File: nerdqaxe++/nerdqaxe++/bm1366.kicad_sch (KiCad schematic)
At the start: 78 parts, among them J2 Conn_01x06, U19 BM1370_mode1, U20 BM1370_mode1, U25 BM1370_mode1, U26 BM1370_mode1, U35 TXU0304PW, U8 25MHz

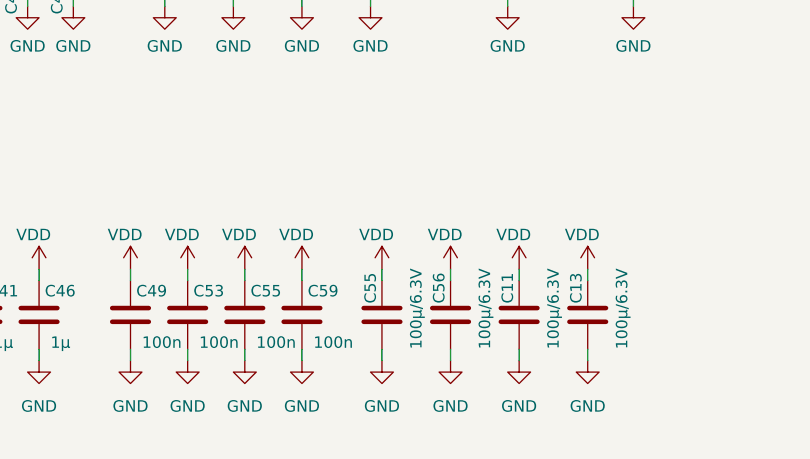
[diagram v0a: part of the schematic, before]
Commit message: removed solderjumpers on ++
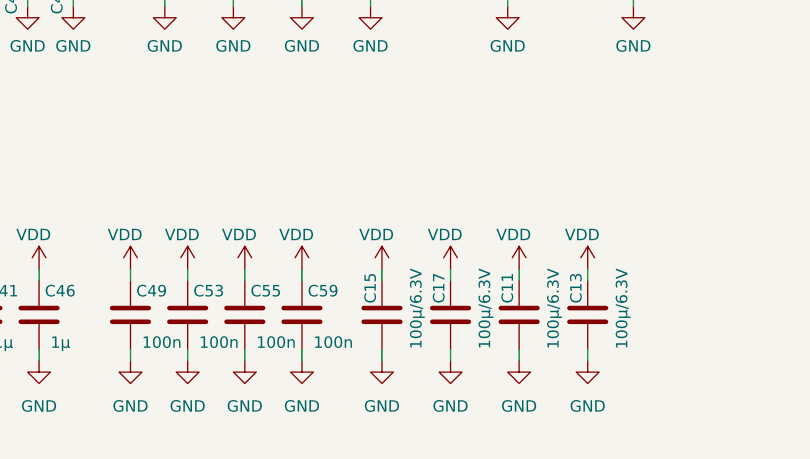
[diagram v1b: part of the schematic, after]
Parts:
- U35: footprint Package_SO:TSSOP-14_4.4x5mm_P0.65mm -> Package_SO:TSSOP-14_4.4x5mm_P0.65mm
- renumbered C55 to C15, C56 to C17
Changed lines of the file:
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@@
 (kicad_sch
-	(version 20231120)
+	(version 20250114)
 	(generator "eeschema")
-	(generator_version "8.0")
+	(generator_version "9.0")
 	(paper "A3")
 	(title_block
@@
 	(label "RO"
 		(at 337.82 55.88 180)
-		(fields_autoplaced yes)
 		(effects
 			(font
@@
 	(label "RESET"
 		(at 365.76 50.8 0)
-		(fields_autoplaced yes)
 		(effects
 			(font
@@
 	(label "RST_N"
 		(at 261.62 241.3 180)
-		(fields_autoplaced yes)
 		(effects
 			(font
@@
 	(label "RO"
 		(at 101.6 66.04 0)
-		(fields_autoplaced yes)
 		(effects
 			(font
@@
 	(label "CI"
 		(at 260.35 246.38 180)
-		(fields_autoplaced yes)
 		(effects
 			(font
@@
 	(label "CLKI"
 		(at 101.6 68.58 0)
-		(fields_autoplaced yes)
 		(effects
 			(font
@@
 	(label "TXD"
 		(at 30.48 44.45 0)
-		(fields_autoplaced yes)
 		(effects
 			(font
@@
 	(label "RXD"
 		(at 30.48 41.91 0)
-		(fields_autoplaced yes)
 		(effects
 			(font
@@
 	(label "RST_N"
 		(at 101.6 60.96 0)
-		(fields_autoplaced yes)
 		(effects
 			(font
@@
 	(label "TXD"
 		(at 365.76 48.26 0)
-		(fields_autoplaced yes)
 		(effects
 			(font
@@
 	(label "RST_N"
 		(at 337.82 50.8 180)
-		(fields_autoplaced yes)
 		(effects
 			(font
@@
 	(label "RXD"
 		(at 365.76 55.88 0)
-		(fields_autoplaced yes)
 		(effects
 			(font
@@
 	(label "RESET"
 		(at 30.48 46.99 0)
-		(fields_autoplaced yes)
 		(effects
 			(font
@@
 	(label "RO"
 		(at 261.62 243.84 180)
-		(fields_autoplaced yes)
 		(effects
 			(font
@@
 	(label "BI"
 		(at 101.6 71.12 0)
-		(fields_autoplaced yes)
 		(effects
 			(font
@@
 	(label "CI"
 		(at 101.6 63.5 0)
-		(fields_autoplaced yes)
 		(effects
 			(font
@@
 	(label "CI"
 		(at 337.82 48.26 180)
-		(fields_autoplaced yes)
 		(effects
 			(font
@@
 		(shape input)
 		(at 29.21 31.75 180)
-		(fields_autoplaced yes)
 		(effects
 			(font
@@
 		(shape input)
 		(at 29.21 39.37 180)
-		(fields_autoplaced yes)
 		(effects
 			(font
@@
 		(shape input)
 		(at 29.21 36.83 180)
-		(fields_autoplaced yes)
 		(effects
 			(font
@@
 		(shape output)
 		(at 29.21 44.45 180)
-		(fields_autoplaced yes)
 		(effects
 			(font
@@
 		(shape output)
 		(at 29.21 46.99 180)
-		(fields_autoplaced yes)
 		(effects
 			(font
@@
 		(shape input)
 		(at 29.21 34.29 180)
-		(fields_autoplaced yes)
 		(effects
 			(font
@@
 		(shape input)
 		(at 29.21 41.91 180)
-		(fields_autoplaced yes)
 		(effects
 			(font
@@
 			)
 		)
-		(property "Footprint" "Package_SO:TSSOP-14_4.4x5mm_P0.65mm "
+		(property "Footprint" "Package_SO:TSSOP-14_4.4x5mm_P0.65mm"
 			(at 360.68 48.26 0)
 			(effects
@@
 		(on_board yes)
 		(dnp no)
-		(property "Reference" "C55"
+		(property "Reference" "C15"
 			(at 137.16 241.3 90)
 			(effects
@@
 		(on_board yes)
 		(dnp no)
-		(property "Reference" "C56"
+		(property "Reference" "C17"
 			(at 144.78 241.3 90)
 			(effects

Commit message: rev5.1.1
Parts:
- C11, C13, C15, C17: value 100µ/6.3V -> 100µ/10V; temp-coefficient (none) -> X5R
- C25, C49, C53, C55, C59, C82, C83: Distributor (none) -> D; Manufacturer (none) -> C0805C104K5RACTU; OrderNr (none) -> 399-C0805C104K5RACTUCT-ND; temp-coefficient (none) -> X7R
- C26, C27, C29, C31: value 10µ -> 10µ/25V; Manufacturer C2012X5R1E106K125AB -> GRM21BZ71E106KE15L; OrderNr 445-5984-1-ND -> 490-GRM21BZ71E106KE15LCT-ND; temp-coefficient (none) -> X7R
- C28, C30, C32, C33, C34, C35, C36, C37, C38, C40, C41, C42, C43, C44, C46, C47, C50, C51, C52, C54, C56, C57, C58, C60, C62, C63, C64, C66, C67, C68, C69, C70, C71, C72, C73, C74, C75, C76, C77, C78, C79, C80, C93, C94: value 1µ -> 1µ/25V; Distributor (none) -> D; Manufacturer (none) -> CL21B105KBFNNNE; OrderNr (none) -> 1276-1029-1-ND; temp-coefficient (none) -> X7R
- R19, R20, R21, R22, R23: Distributor (none) -> D; Manufacturer (none) -> RMCF0805FT10K0; OrderNr (none) -> RMCF0805FT10K0CT-ND
- R44, R45, R46, R47: Distributor (none) -> D; Manufacturer (none) -> RNCP0805FTD1K00; OrderNr (none) -> RNCP0805FTD1K00CT-ND
- R49, R50, R51: Distributor (none) -> D; Manufacturer (none) -> CRG0805F2K0; OrderNr (none) -> A126358CT-ND
